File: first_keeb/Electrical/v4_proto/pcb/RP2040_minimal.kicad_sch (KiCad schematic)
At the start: 60 parts, among them P1 USB4105-GF-A, Q1 SN74LV1T34DBV, SW1 SW_Push, SW2 SW_Push, SW3 SKRKAGE020, U1 NCP1117-3.3_SOT223, U2 LM4040DBZ-3, U3 PRTR5V0U2X, U4 W25Q32JVSS, U5 RP2040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

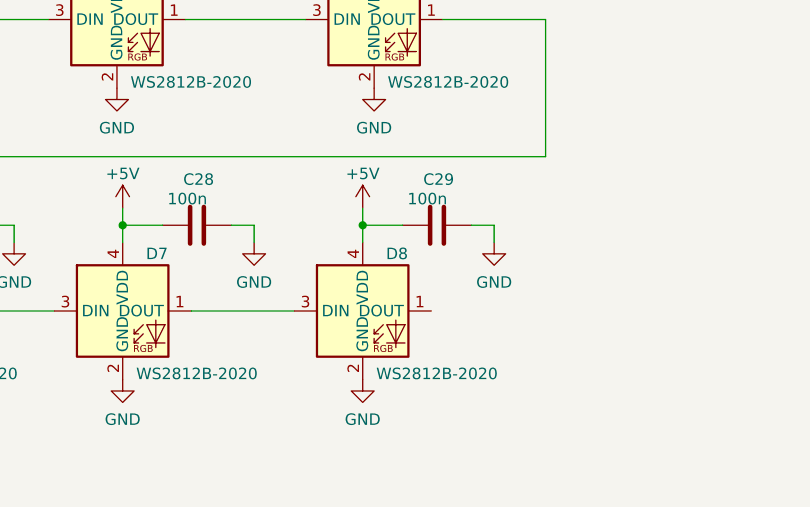
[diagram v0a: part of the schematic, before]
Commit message: removes extra led
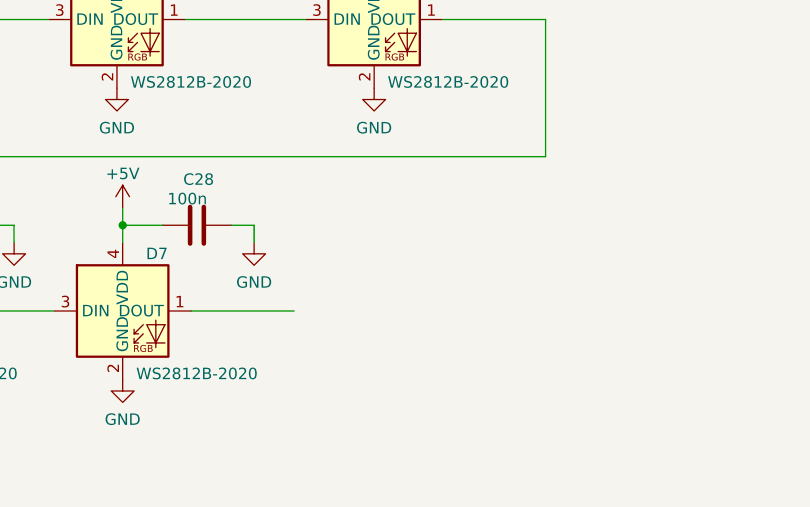
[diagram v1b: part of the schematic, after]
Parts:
- removed C29: 100n, Capacitor_SMD:C_0402_1005Metric, symbol Device:C
- removed D8: WS2812B-2020, LED_SMD:LED_WS2812B-2020_PLCC4_2.0x2.0mm, symbol LED:WS2812B-2020
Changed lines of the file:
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@@
   (junction (at 175.895 226.06) (diameter 0) (color 0 0 0 0)
   )
-  (junction (at 266.7 248.92) (diameter 0) (color 0 0 0 0)
-  )
   (junction (at 105.41 36.83) (diameter 0) (color 0 0 0 0)
   )
@@
     (stroke (width 0) (type default))
   )
-  (wire (pts (xy 281.305 248.92) (xy 278.765 248.92))
-    (stroke (width 0) (type default))
-  )
   (wire (pts (xy 128.27 38.1) (xy 128.27 36.83))
     (stroke (width 0) (type default))
@@
     (stroke (width 0) (type default))
   )
-  (wire (pts (xy 266.7 248.92) (xy 271.145 248.92))
-    (stroke (width 0) (type default))
-  )
   (wire (pts (xy 81.28 209.55) (xy 81.28 210.82))
     (stroke (width 0) (type default))
@@
     (stroke (width 0) (type default))
   )
-  (wire (pts (xy 281.305 248.92) (xy 281.305 250.825))
-    (stroke (width 0) (type default))
-  )
   (wire (pts (xy 80.01 171.45) (xy 80.01 173.99))
     (stroke (width 0) (type default))
@@
     (stroke (width 0) (type default))
   )
-  (wire (pts (xy 266.7 247.015) (xy 266.7 248.92))
-    (stroke (width 0) (type default))
-  )
   (wire (pts (xy 277.495 117.475) (xy 260.985 117.475))
     (stroke (width 0) (type default))
@@
     (stroke (width 0) (type default))
   )
-  (wire (pts (xy 266.7 248.92) (xy 266.7 250.825))
-    (stroke (width 0) (type default))
-  )
   (wire (pts (xy 111.76 146.05) (xy 127 146.05))
     (stroke (width 0) (type default))
@@
     )
   )
-  (symbol (lib_id "LED:WS2812B-2020") (at 266.7 258.445 0) (unit 1)
-    (in_bom yes) (on_board yes) (dnp no)
-    (property "Reference" "D8" (at 270.51 252.095 0)
-      (effects (font (size 1.27 1.27)))
-    )
-    (property "Value" "WS2812B-2020" (at 274.955 265.43 0)
-      (effects (font (size 1.27 1.27)))
-    )
-    (property "Footprint" "LED_SMD:LED_WS2812B-2020_PLCC4_2.0x2.0mm" (at 265.43 266.065 0)
-      (effects (font (size 1.27 1.27)) hide)
-    )
-    (property "Datasheet" "" (at 266.7 258.445 0)
-      (effects (font (size 1.27 1.27)) hide)
-    )
-    (pin "1")
-    (pin "2")
-    (pin "3")
-    (pin "4")
-    (instances
-      (project "RP2040_minimal"
-        (path "/26e500cb-9f3f-4e62-bb26-21a6be4a5bcc"
-          (reference "D8") (unit 1)
-        )
-      )
-    )
-  )
   (symbol (lib_id "Device:C") (at 193.04 248.92 90) (unit 1)
     (in_bom yes) (on_board yes) (dnp no)
@@
     )
   )
-  (symbol (lib_name "GND_1") (lib_id "power:GND") (at 266.7 266.065 0) (unit 1)
-    (in_bom yes) (on_board yes) (dnp no) (fields_autoplaced)
-    (property "Reference" "#PWR063" (at 266.7 272.415 0)
-      (effects (font (size 1.27 1.27)) hide)
-    )
-    (property "Value" "GND" (at 266.7 270.51 0)
-      (effects (font (size 1.27 1.27)))
-    )
-    (property "Footprint" "" (at 266.7 266.065 0)
-      (effects (font (size 1.27 1.27)) hide)
-    )
-    (property "Datasheet" "" (at 266.7 266.065 0)
-      (effects (font (size 1.27 1.27)) hide)
-    )
-    (pin "1")
-    (instances
-      (project "RP2040_minimal"
-        (path "/26e500cb-9f3f-4e62-bb26-21a6be4a5bcc"
-          (reference "#PWR063") (unit 1)
-        )
-      )
-      (project "first_keeb"
-        (path "/e63e39d7-6ac0-4ffd-8aa3-1841a4541b55"
-          (reference "#PWR045") (unit 1)
-        )
-      )
-    )
-  )
   (symbol (lib_id "power:GND") (at 109.22 222.885 0) (unit 1)
     (in_bom yes) (on_board yes) (dnp no)
@@
     )
   )
-  (symbol (lib_name "GND_1") (lib_id "power:GND") (at 281.305 250.825 0) (unit 1)
-    (in_bom yes) (on_board yes) (dnp no) (fields_autoplaced)
-    (property "Reference" "#PWR062" (at 281.305 257.175 0)
-      (effects (font (size 1.27 1.27)) hide)
-    )
-    (property "Value" "GND" (at 281.305 255.27 0)
-      (effects (font (size 1.27 1.27)))
-    )
-    (property "Footprint" "" (at 281.305 250.825 0)
-      (effects (font (size 1.27 1.27)) hide)
-    )
-    (property "Datasheet" "" (at 281.305 250.825 0)
-      (effects (font (size 1.27 1.27)) hide)
-    )
-    (pin "1")
-    (instances
-      (project "RP2040_minimal"
-        (path "/26e500cb-9f3f-4e62-bb26-21a6be4a5bcc"
-          (reference "#PWR062") (unit 1)
-        )
-      )
-      (project "first_keeb"
-        (path "/e63e39d7-6ac0-4ffd-8aa3-1841a4541b55"
-          (reference "#PWR045") (unit 1)
-        )
-      )
-    )
-  )
   (symbol (lib_id "Memory_Flash:W25Q32JVSS") (at 287.655 120.015 0) (unit 1)
     (in_bom yes) (on_board yes) (dnp no) (fields_autoplaced)
@@
     )
   )
-  (symbol (lib_id "Device:C") (at 274.955 248.92 90) (unit 1)
-    (in_bom yes) (on_board yes) (dnp no)
-    (property "Reference" "C29" (at 276.86 243.84 90)
-      (effects (font (size 1.27 1.27)) (justify left))
-    )
-    (property "Value" "100n" (at 276.098 245.999 90)
-      (effects (font (size 1.27 1.27)) (justify left))
-    )
-    (property "Footprint" "Capacitor_SMD:C_0402_1005Metric" (at 278.765 247.9548 0)
-      (effects (font (size 1.27 1.27)) hide)
-    )
-    (property "Datasheet" "~" (at 274.955 248.92 0)
-      (effects (font (size 1.27 1.27)) hide)
-    )
-    (pin "1")
-    (pin "2")
-    (instances
-      (project "RP2040_minimal"
-        (path "/26e500cb-9f3f-4e62-bb26-21a6be4a5bcc"
-          (reference "C29") (unit 1)
-        )
-      )
-    )
-  )
   (symbol (lib_id "Device:C") (at 247.65 216.535 90) (unit 1)
     (in_bom yes) (on_board yes) (dnp no)
@@
         )
       )
-    )
-  )
-  (symbol (lib_id "power:+5V") (at 266.7 247.015 0) (unit 1)
-    (in_bom yes) (on_board yes) (dnp no)
-    (property "Reference" "#PWR059" (at 266.7 250.825 0)
-      (effects (font (size 1.27 1.27)) hide)
-    )
-    (property "Value" "+5V" (at 266.7 243.205 0)
-      (effects (font (size 1.27 1.27)))
-    )
-    (property "Footprint" "" (at 266.7 247.015 0)
-      (effects (font (size 1.27 1.27)) hide)
-    )
-    (property "Datasheet" "" (at 266.7 247.015 0)
-      (effects (font (size 1.27 1.27)) hide)
-    )
-    (pin "1")
-    (instances
-      (project "RP2040_minimal"
-        (path "/26e500cb-9f3f-4e62-bb26-21a6be4a5bcc"
-          (reference "#PWR059") (unit 1)
-        )
-      )

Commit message: adds stl file
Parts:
- added H1, H2, H3, H4, H5, H6, H7: 4881_M3_Threaded_Insert, MountingHole:4881_M3_Threaded_Insert, symbol Mechanical:4881
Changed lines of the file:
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@@
+    )
+  )
+  (symbol (lib_id "Mechanical:4881") (at 349.885 44.45 0) (unit 1)
+    (in_bom yes) (on_board yes) (dnp no) (fields_autoplaced)
+    (property "Reference" "H4" (at 353.06 42.545 0)
+      (effects (font (size 1.27 1.27)) (justify left))
+    )
+    (property "Value" "4881_M3_Threaded_Insert" (at 353.06 45.085 0)
+      (effects (font (size 1.27 1.27)) (justify left))
+    )
+    (property "Footprint" "MountingHole:4881_M3_Threaded_Insert" (at 349.885 44.45 0)
+      (effects (font (size 1.27 1.27)) hide)
+    )
+    (property "Datasheet" "~" (at 349.885 44.45 0)
+      (effects (font (size 1.27 1.27)) hide)
+    )
+    (pin "1")
+    (instances
+      (project "RP2040_minimal"
+        (path "/26e500cb-9f3f-4e62-bb26-21a6be4a5bcc"
+          (reference "H4") (unit 1)
+        )
+      )
     )
   )
@@
         (path "/26e500cb-9f3f-4e62-bb26-21a6be4a5bcc"
           (reference "#PWR011") (unit 1)
+        )
+      )
+    )
+  )
+  (symbol (lib_id "Mechanical:4881") (at 349.885 35.56 0) (unit 1)
+    (in_bom yes) (on_board yes) (dnp no) (fields_autoplaced)
+    (property "Reference" "H3" (at 353.06 33.655 0)
+      (effects (font (size 1.27 1.27)) (justify left))
+    )
+    (property "Value" "4881_M3_Threaded_Insert" (at 353.06 36.195 0)
+      (effects (font (size 1.27 1.27)) (justify left))
+    )
+    (property "Footprint" "MountingHole:4881_M3_Threaded_Insert" (at 349.885 35.56 0)
+      (effects (font (size 1.27 1.27)) hide)
+    )
+    (property "Datasheet" "~" (at 349.885 35.56 0)
+      (effects (font (size 1.27 1.27)) hide)
+    )
+    (pin "1")
+    (instances
+      (project "RP2040_minimal"
+        (path "/26e500cb-9f3f-4e62-bb26-21a6be4a5bcc"
+          (reference "H3") (unit 1)
         )
       )
@@
         (path "/26e500cb-9f3f-4e62-bb26-21a6be4a5bcc"
           (reference "D1") (unit 1)
+        )
+      )
+    )
+  )
+  (symbol (lib_id "Mechanical:4881") (at 349.885 64.135 0) (unit 1)
+    (in_bom yes) (on_board yes) (dnp no) (fields_autoplaced)
+    (property "Reference" "H6" (at 353.06 62.23 0)
+      (effects (font (size 1.27 1.27)) (justify left))
+    )
+    (property "Value" "4881_M3_Threaded_Insert" (at 353.06 64.77 0)
+      (effects (font (size 1.27 1.27)) (justify left))
+    )
+    (property "Footprint" "MountingHole:4881_M3_Threaded_Insert" (at 349.885 64.135 0)
+      (effects (font (size 1.27 1.27)) hide)
+    )
+    (property "Datasheet" "~" (at 349.885 64.135 0)
+      (effects (font (size 1.27 1.27)) hide)
+    )
+    (pin "1")
+    (instances
+      (project "RP2040_minimal"
+        (path "/26e500cb-9f3f-4e62-bb26-21a6be4a5bcc"
+          (reference "H6") (unit 1)
         )
       )
@@
         (path "/26e500cb-9f3f-4e62-bb26-21a6be4a5bcc"
           (reference "U2") (unit 1)
+        )
+      )
+    )
+  )
+  (symbol (lib_id "Mechanical:4881") (at 349.885 54.61 0) (unit 1)
+    (in_bom yes) (on_board yes) (dnp no) (fields_autoplaced)
+    (property "Reference" "H5" (at 353.06 52.705 0)
+      (effects (font (size 1.27 1.27)) (justify left))
+    )
+    (property "Value" "4881_M3_Threaded_Insert" (at 353.06 55.245 0)
+      (effects (font (size 1.27 1.27)) (justify left))
+    )
+    (property "Footprint" "MountingHole:4881_M3_Threaded_Insert" (at 349.885 54.61 0)
+      (effects (font (size 1.27 1.27)) hide)
+    )
+    (property "Datasheet" "~" (at 349.885 54.61 0)
+      (effects (font (size 1.27 1.27)) hide)
+    )
+    (pin "1")
+    (instances
+      (project "RP2040_minimal"
+        (path "/26e500cb-9f3f-4e62-bb26-21a6be4a5bcc"
+          (reference "H5") (unit 1)
         )
       )
@@
     )
   )
+  (symbol (lib_id "Mechanical:4881") (at 349.885 26.67 0) (unit 1)
+    (in_bom yes) (on_board yes) (dnp no) (fields_autoplaced)
+    (property "Reference" "H2" (at 353.06 24.765 0)
+      (effects (font (size 1.27 1.27)) (justify left))
+    )
+    (property "Value" "4881_M3_Threaded_Insert" (at 353.06 27.305 0)
+      (effects (font (size 1.27 1.27)) (justify left))
+    )
+    (property "Footprint" "MountingHole:4881_M3_Threaded_Insert" (at 349.885 26.67 0)
+      (effects (font (size 1.27 1.27)) hide)
+    )
+    (property "Datasheet" "~" (at 349.885 26.67 0)
+      (effects (font (size 1.27 1.27)) hide)
+    )
+    (pin "1")
+    (instances
+      (project "RP2040_minimal"
+        (path "/26e500cb-9f3f-4e62-bb26-21a6be4a5bcc"
+          (reference "H2") (unit 1)
+        )
+      )
+    )
+  )
   (symbol (lib_id "power:+3V3") (at 186.055 37.465 0) (unit 1)
     (in_bom yes) (on_board yes) (dnp no)
@@
         (path "/26e500cb-9f3f-4e62-bb26-21a6be4a5bcc"
           (reference "#PWR042") (unit 1)
+        )
+      )
+    )
+  )
+  (symbol (lib_id "Mechanical:4881") (at 349.885 18.415 0) (unit 1)
+    (in_bom yes) (on_board yes) (dnp no) (fields_autoplaced)
+    (property "Reference" "H1" (at 353.06 16.51 0)
+      (effects (font (size 1.27 1.27)) (justify left))
+    )
+    (property "Value" "4881_M3_Threaded_Insert" (at 353.06 19.05 0)
+      (effects (font (size 1.27 1.27)) (justify left))
+    )
+    (property "Footprint" "MountingHole:4881_M3_Threaded_Insert" (at 349.885 18.415 0)
+      (effects (font (size 1.27 1.27)) hide)
+    )
+    (property "Datasheet" "~" (at 349.885 18.415 0)
+      (effects (font (size 1.27 1.27)) hide)
+    )
+    (pin "1")
+    (instances
+      (project "RP2040_minimal"
+        (path "/26e500cb-9f3f-4e62-bb26-21a6be4a5bcc"
+          (reference "H1") (unit 1)
         )
       )
@@
         )
       )
+    )
+  )
+  (symbol (lib_id "Mechanical:4881") (at 349.885 73.66 0) (unit 1)
+    (in_bom yes) (on_board yes) (dnp no) (fields_autoplaced)
+    (property "Reference" "H7" (at 353.06 71.755 0)
+      (effects (font (size 1.27 1.27)) (justify left))
+    )
+    (property "Value" "4881_M3_Threaded_Insert" (at 353.06 74.295 0)
+      (effects (font (size 1.27 1.27)) (justify left))
+    )
+    (property "Footprint" "MountingHole:4881_M3_Threaded_Insert" (at 349.885 73.66 0)
+      (effects (font (size 1.27 1.27)) hide)
+    )
+    (property "Datasheet" "~" (at 349.885 73.66 0)
+      (effects (font (size 1.27 1.27)) hide)
+    )
+    (pin "1")
+    (instances
+      (project "RP2040_minimal"
+        (path "/26e500cb-9f3f-4e62-bb26-21a6be4a5bcc"
+          (reference "H7") (unit 1)
+        )
+      )
